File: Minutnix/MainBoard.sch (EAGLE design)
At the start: 84 parts, among them IC1 MEGA8-AI, IC2 TPIC6C596PW, IC3 TPIC6C596PW, IC4 TPIC6C596PW, IC5 TPIC6C596PW, Q1 32.768kHz

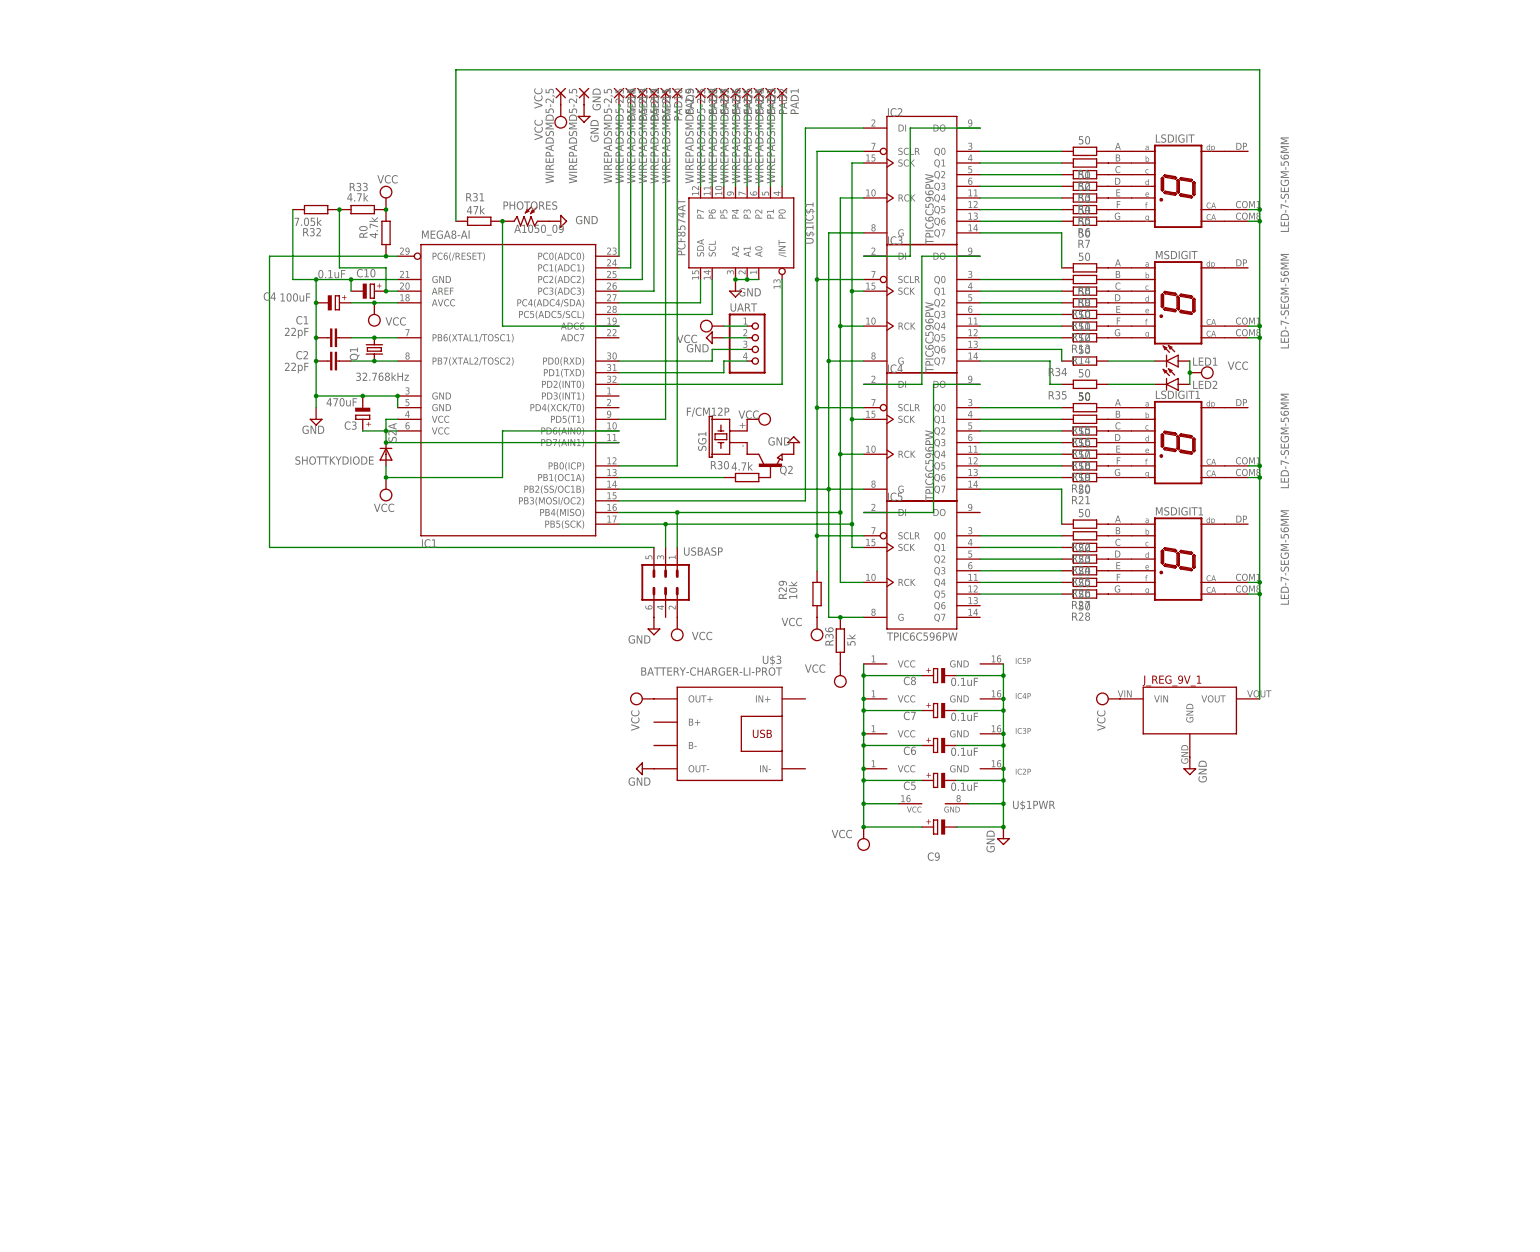
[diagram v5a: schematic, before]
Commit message: Power boards incorporated
Redrawn power supply  circuits so we use one PCB
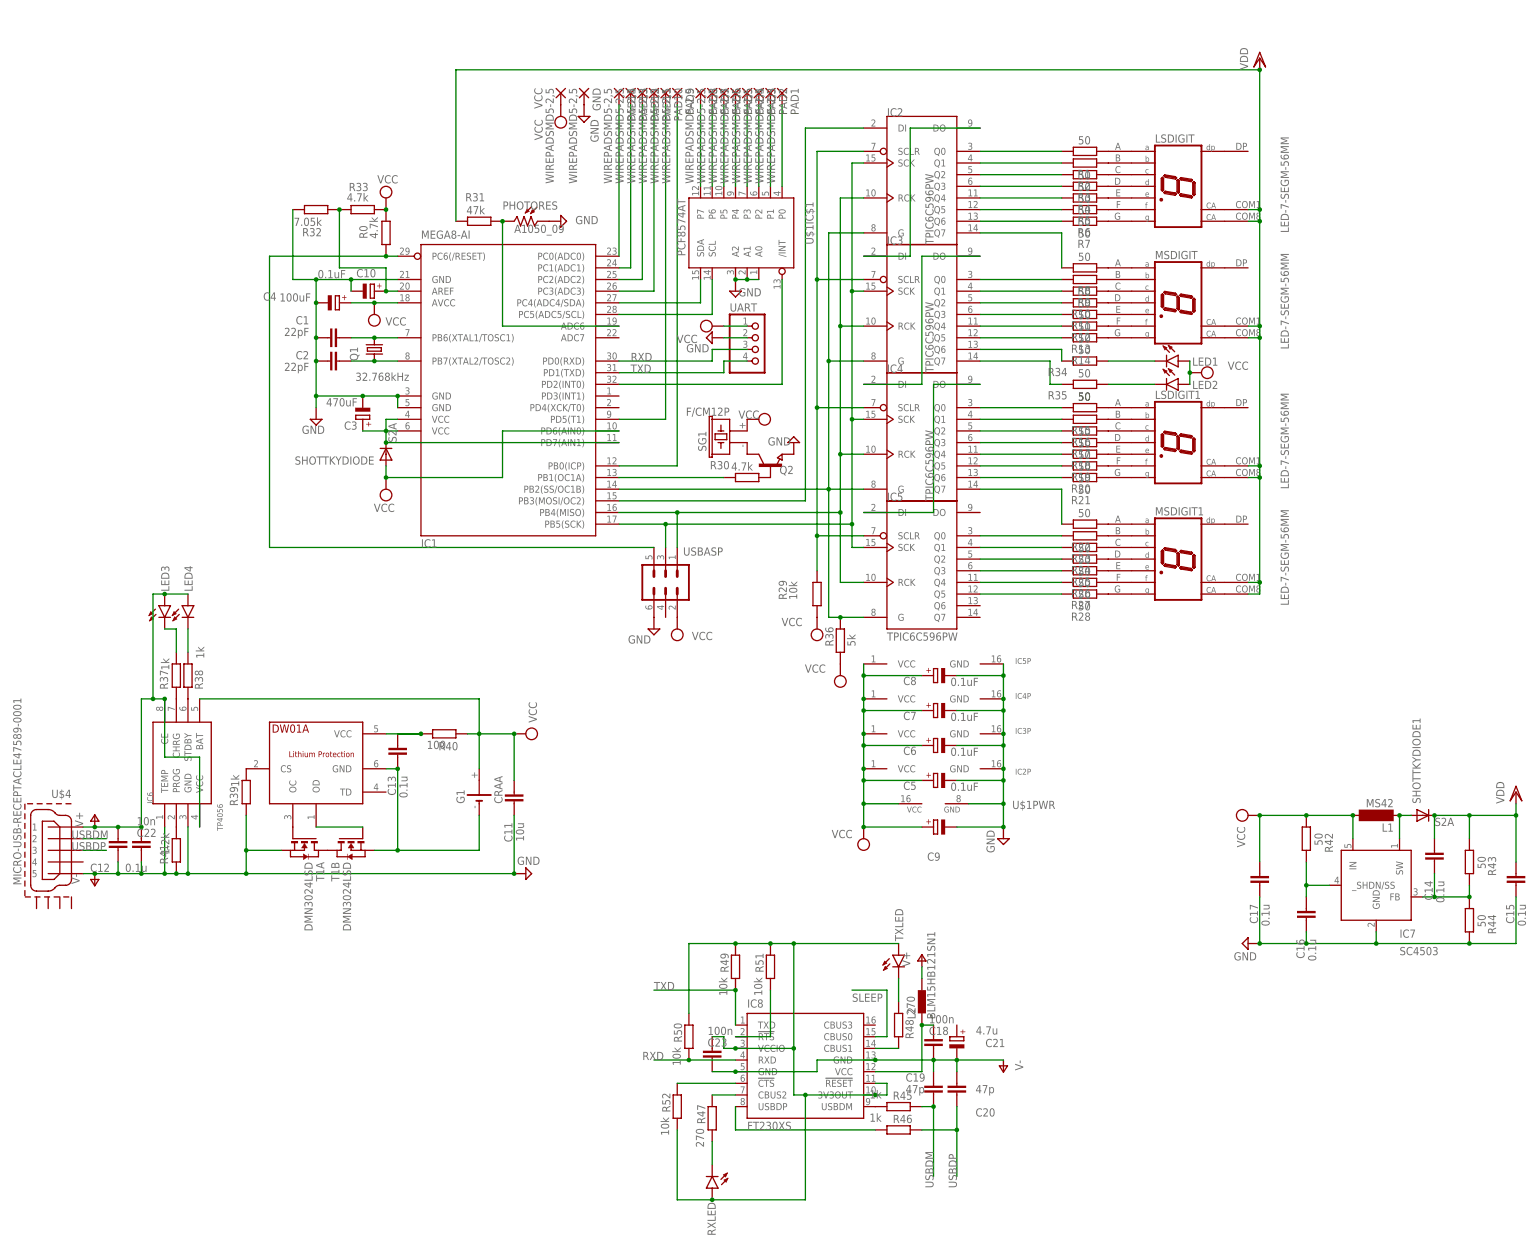
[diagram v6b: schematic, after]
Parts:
- removed J_REG_9V_1: 9V_VOLTAGE_REGULATOR, PololuVreg:9V_VOLTAGE_REGULATOR
- removed U$3: BATTERY-CHARGER-LI-PROT, diy-modules:BATTERY-CHARGER-LI-PROT
- added C11: 10u, capacitor-wima:C2.5/2
- added C12, C13, C14, C15, C16, C17: 0.1u, capacitor-wima:C2.5/2
- added C18, C23: 100n, capacitor-wima:C2.5/2
- added C19, C20: 47p, capacitor-wima:C2.5/2
- added C21: 4.7u, rcl:CPOL-EU140CLH-1010
- added C22: 10n, capacitor-wima:C2.5/2
- added G1: CRAA, battery:CRAA
- added IC6: TP4056, TP4056:TP4056
- added IC7: SC4503, v-reg-3:SC4503
- added IC8: FT230XS, ftdi:FT230XS
- added L1: MS42, inductor-neosid:MS42
- added L2: BLM15HB121SN1, inductors:BLM15HB121SN1
- added LED3, LED4, RXLED, TXLED: (no value), led:LED5MM
- added R37, R38, R39, R45, R46: 1k, rcl:R-EU_R1206
- added R40: 100, rcl:R-EU_R1206
- added R41: 1.2k, rcl:R-EU_R1206
- added R42, R43, R44: 50, rcl:R-EU_R1206
- added R47, R48: 270, rcl:R-EU_R1206
- added R49, R50, R51, R52: 10k, rcl:R-EU_R1206
- added SHOTTKYDIODE1: S2A, s2x_10:S2A
- added T1: DMN3024LSD, FS8205A:DMN3024LSD
- added U$2: DW01A, DW01A:DW01A
- added U$4: MICRO-USB-RECEPTACLE47589-0001, con-molex-usb:MICRO-USB-RECEPTACLE47589-0001
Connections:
- new net N$100: LED3.C, R37.2
- new net N$101: LED4.C, R38.2
- new net N$102: T1A.G, U$2.OC
- new net N$103: IC8.USBDM, R45.2
- new net N$104: T1A.D, T1B.D
- new net N$105: T1B.G, U$2.OD
- new net N$106: R39.2, U$2.CS
- new net N$107: IC7.SW, L1.1, SHOTTKYDIODE1.A
- new net N$108: C13.1, G1.-, T1B.S, U$2.GND
- new net N$109: C13.2, R40.2, U$2.VCC
- new net N$110: C16.2, IC7._SHDN/SS, R42.2
- new net N$111: IC6.PROG, R41.2
- new net N$112: C14.1, IC7.FB, R43.2, R44.1
- new net N$114: R47.2, RXLED.C
- new net N$115: IC8.CBUS2, R47.1
- new net N$116: R48.2, TXLED.C
- new net N$117: IC8.CBUS1, R48.1
- new net N$98: IC6.CHRG, R37.1
- new net N$99: IC6.STDBY, R38.1
- new net RXD: IC1.PD0(RXD), IC8.RXD, R50.2, UART.3
- new net SLEEP: IC8.CBUS0
- new net TXD: IC1.PD1(TXD), IC8.TXD, R49.2, UART.4
- new net USBDM: C19.1, R45.1, U$4.2
- new net USBDP: C20.1, R46.1, U$4.3
- new net V+: C12.2, C18.2, C22.2, IC6.CE, IC6.VCC, IC8.VCC, L2.1, L2.2, LED3.A, LED4.A, U$4.1
- new net V+2: C23.2, IC8.!RESET, IC8.3V3OUT, IC8.VCCIO, R49.1, R50.1, R51.1, R52.2, RXLED.A, TXLED.A
- new net V-: C11.1, C12.1, C18.1, C19.2, C20.2, C21.-, C22.1, C23.1, IC6.GND, IC6.TEMP, IC8.GND, IC8.GND@1, R39.1, R41.1, T1A.S, U$4.5
- new net VDD: C14.2, C15.2, LSDIGIT.CA1, LSDIGIT.CA8, LSDIGIT1.CA1, LSDIGIT1.CA8, MSDIGIT.CA1, MSDIGIT.CA8, MSDIGIT1.CA1, MSDIGIT1.CA8, R31.2, R43.1, SHOTTKYDIODE1.C
- net GND: now also C15.1, C16.1, C17.1, IC7.GND, R44.2; no longer J_REG_9V_1.GND, U$3.OUT-
- net N$28: now also IC8.USBDP, R46.2; no longer J_REG_9V_1.VOUT, LSDIGIT.CA1, LSDIGIT.CA8, LSDIGIT1.CA1, LSDIGIT1.CA8, MSDIGIT.CA1, MSDIGIT.CA8, MSDIGIT1.CA1, MSDIGIT1.CA8, R31.2
- net N$30: now also IC8.!RTS, R51.2; no longer IC1.PD1(TXD), UART.4
- net N$31: now also IC8.!CTS, R52.1; no longer IC1.PD0(RXD), UART.3
- net VCC: now also C11.2, C17.2, G1.+, IC6.BAT, IC7.IN, L1.2, R40.1, R42.1; no longer J_REG_9V_1.VIN, U$3.OUT+

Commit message: Newest Corrected schematic
Splited into diffrent sheets. Improoved readability.
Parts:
- removed C14, C15, C16, C17: 0.1u, capacitor-wima:C2.5/2
- removed GND, VCC: WIREPADSMD5-2,5, wirepad:WIREPADSMD5-2,5
- removed IC7: SC4503, v-reg-3:SC4503
- removed L1: MS42, inductor-neosid:MS42
- removed R42, R43, R44: 50, rcl:R-EU_R1206
- removed SHOTTKYDIODE1: S2A, s2x_10:S2A
- removed U$4: MICRO-USB-RECEPTACLE47589-0001, con-molex-usb:MICRO-USB-RECEPTACLE47589-0001
- removed UART: (no value), pinhead:PINHD-1X4
- removed USBASP: (no value), con-harting-ml:ML6
- added B_GND, B_VCC: WIREPADSMD5-2,5, wirepad:WIREPADSMD5-2,5
- added C24, C25, C26, C27: 0.1u, capacitor-wima:C2.5/2
- added IC10, IC11, IC12, IC13: TPIC6C596PW, tpic:TPIC6C596PW
- added IC9: SC4503, v-reg-3:SC4503
- added L3: MS42, inductor-neosid:MS42
- added MICROUSB: MICRO-USB-RECEPTACLE47589-0001, con-molex-usb:MICRO-USB-RECEPTACLE47589-0001
- added R53, R54, R55: 50, rcl:R-EU_R1206
- added SHOTTKYDIODE2: S2A, s2x_10:S2A
- added U$3: PCF8574AT, i2c:PCF8574AT
- C10: value 0.1uF -> 100nF
- R34, R35: value 50 -> 200
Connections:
- net N$12 renamed L6
- net N$14 renamed L5
- net N$20 renamed L4
- net N$23 renamed D_SI
- net N$3 renamed BUZZ
- net N$33 renamed EXP_SDA
- net N$36 renamed EXP_INT
- net N$4 renamed D_BLOCK
- net N$81 renamed EXP_SCL
- net N$82 renamed L3
- net N$83 renamed L1
- net N$84 renamed L2
- net N$85 renamed B1
- net N$86 renamed B2
- net N$87 renamed B3
- net N$88 renamed B4
- net N$89 renamed B5
- net N$90 renamed B6
- net N$91 renamed ENC_A
- net N$92 renamed ENC_B
- net N$93 renamed LIGHT_SENS
- removed net N$107: IC7.SW, L1.1, SHOTTKYDIODE1.A
- removed net N$110: C16.2, IC7._SHDN/SS, R42.2
- removed net N$112: C14.1, IC7.FB, R43.2, R44.1
- removed net N$26: IC1.PB5(SCK), IC2G$1.SCK, IC3G$1.SCK, IC4G$1.SCK, IC5G$1.SCK, USBASP.3
- removed net N$27: IC1.PB4(MISO), IC2G$1.RCK, IC3G$1.RCK, IC4G$1.RCK, IC5G$1.RCK, USBASP.1
- removed net SLEEP: IC8.CBUS0
- removed net V+: C12.2, C18.2, C22.2, IC6.CE, IC6.VCC, IC8.VCC, L2.1, L2.2, LED3.A, LED4.A, U$4.1
- removed net V+2: C23.2, IC8.!RESET, IC8.3V3OUT, IC8.VCCIO, R49.1, R50.1, R51.1, R52.2, RXLED.A, TXLED.A
- removed net V-: C11.1, C12.1, C18.1, C19.2, C20.2, C21.-, C22.1, C23.1, IC6.GND, IC6.TEMP, IC8.GND, IC8.GND@1, R39.1, R41.1, T1A.S, U$4.5
- new net +3V3: C23.2, IC8.!RESET, IC8.3V3OUT, IC8.VCCIO, R49.2, R50.2, R51.1, R52.2, RXLED.A, TXLED.A
- new net +5V: C12.2, C18.2, C21.+, IC6.CE, IC6.VCC, IC8.VCC, L2.1, LED3.A, LED4.A
- new net D_RCK: IC1.PB4(MISO), IC2G$1.RCK, IC3G$1.RCK, IC4G$1.RCK, IC5G$1.RCK
- new net D_SCK: IC1.PB5(SCK), IC2G$1.SCK, IC3G$1.SCK, IC4G$1.SCK, IC5G$1.SCK
- new net N$113: IC9.SW, L3.1, SHOTTKYDIODE2.A
- new net N$118: C26.2, IC9._SHDN/SS, R53.2
- new net N$119: C24.1, IC9.FB, R54.2, R55.1
- new net N$14: C22.2, L2.2, MICROUSB.1
- new net N$4: C4.+, IC1.AVCC
- net GND: now also B_GND.P, C11.1, C12.1, C18.1, C19.2, C20.1, C21.-, C22.1, C23.1, C25.1, C26.1, C27.1, IC10P.GND, IC11P.GND, IC12P.GND, IC13P.GND, IC6.GND, IC6.TEMP, IC8.GND, IC8.GND@1, IC9.GND, MICROUSB.5, R39.1, R41.1, R55.2, T1A.S, U$3PWR.GND; no longer C15.1, C16.1, C17.1, GND.P, IC2P.GND, IC3P.GND, IC4P.GND, IC5P.GND, IC7.GND, R44.2, U$1PWR.GND, UART.2, USBASP.6
- net N$22: no longer USBASP.5
- net RXD: now also R50.1; no longer R50.2, UART.3
- net TXD: now also R49.1; no longer R49.2, UART.4
- net USBDM: now also MICROUSB.2; no longer U$4.2
- net USBDP: now also C20.2, MICROUSB.3; no longer C20.1, U$4.3
- net VCC: now also B_VCC.P, C27.2, IC10P.VCC, IC11P.VCC, IC12P.VCC, IC13P.VCC, IC9.IN, L3.2, R53.1, U$3PWR.VCC; no longer C17.2, C4.+, IC1.AVCC, IC2P.VCC, IC3P.VCC, IC4P.VCC, IC5P.VCC, IC7.IN, L1.2, R42.1, U$1PWR.VCC, UART.1, USBASP.2, VCC.P
- net VDD: now also C24.2, C25.2, R54.1, SHOTTKYDIODE2.C; no longer C14.2, C15.2, R43.1, SHOTTKYDIODE1.C
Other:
- note added: "All 7 segment resistors are 50R"
